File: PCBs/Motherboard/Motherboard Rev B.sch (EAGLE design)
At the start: 36 parts, among them IC1 AD590ZR, IC2 AD590ZR, Q1 32kHZ, U1 Value

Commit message: Updated pin-mappings, added SD card
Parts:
- added C18: 0.1uF, adafruit:C-USC0603
- added C19: 10uF, adafruit:C-USC0603
- added J1: (no value), sdCard:SDCARD
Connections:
- removed net 3.3V: C1.1, C10.1, C11.1, C15.1, C2.1, C3.1, C5.1, C6.1, C7.1, C8.1, C9.1, R4.2, U$1.3V3@2, U$2.RESV, U$2.VDD, U$2.VDDIO, U1.AVCC1, U1.DVCC1, U1.DVCC2, U1.DVCC3
- removed net 5V: C16.1, C17.1, IC1.+, IC2.+, U$1.5V@2
- removed net VCC: R1.2, R3.2, R7.2, R9.2
- new net SW10: C18.1, C2.1, R1.2, R3.2, R7.2, R9.2, U$1.IO.28, U$2.RESV, U$2.VDD
- new net SW5: C16.1, C17.1, IC1.+, IC2.+, U$1.IO.35
- new net SW8: C1.1, C10.1, C11.1, C15.1, C19.1, C3.1, C5.1, C6.1, C7.1, C8.1, C9.1, J1.VDD, R4.2, U$1.IO.30, U$2.VDDIO, U1.AVCC1, U1.DVCC1, U1.DVCC2, U1.DVCC3
- net GND: now also C18.2, C19.2
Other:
- note added: "SD Card Reader"
- moved on the sheet: C15, C16, C17, C2, C3, C4, IC1, IC2, R1, R10, R11, R2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

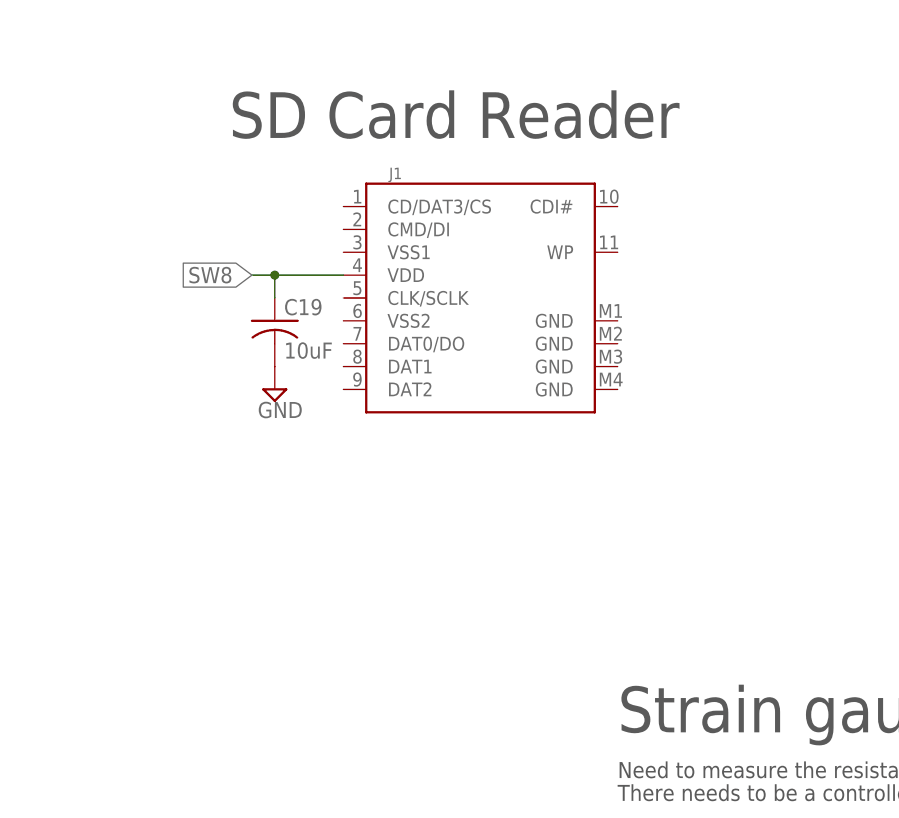
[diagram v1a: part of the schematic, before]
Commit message: Changed SD card connector
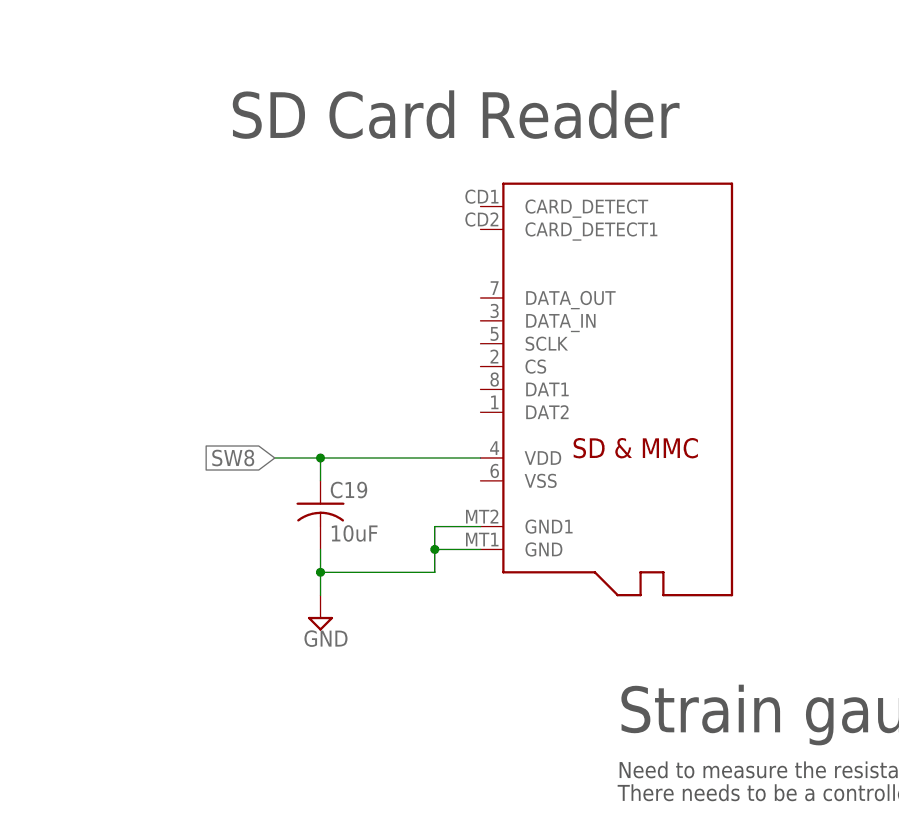
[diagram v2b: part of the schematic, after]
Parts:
- removed J1: (no value), sdCard:SDCARD
- added U$11: MICROSD, adafruit:MICROSD
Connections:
- net GND: now also U$11.GND, U$11.GND1
- net SW8: now also U$11.VDD; no longer J1.VDD
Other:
- moved on the sheet: C19

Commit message: Add temp sensors to GPS and Radio boards
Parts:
- removed IC1, IC2: AD590ZR, linear4:AD590ZR
- removed R10: RCAL, SparkFun-Resistors:12.1KOHM-0603-1/10W-1%
- removed R11: 950, SparkFun-Resistors:12.1KOHM-0603-1/10W-1%
- added R12: RCAL, SparkFun-Resistors:12.1KOHM-0603-1/10W-1%
- added R13: 950, SparkFun-Resistors:12.1KOHM-0603-1/10W-1%
- added X1, X2: OPAMP, ngspice-simulation:OPAMP
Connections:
- removed net N$8: R10.1, R11.2
- new net N$4: R12.1, R13.2
- new net TEMP1: R5.2, U$1.IO.23, X1.P
- new net TEMP2: R12.2, U$1.1O.21, X2.P
- net ADC2: now also X1.N, X1.VOUT; no longer IC1.-, R5.2
- net ADC4: now also X2.N, X2.VOUT; no longer IC2.-, R10.2
- net AGND: now also R13.1; no longer R11.1
- net SW5: no longer IC1.+, IC2.+
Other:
- note added: "AD590KRZ Temp sensor"
- note removed: "AD590KF Temp sensor"
- moved on the sheet: R5, R6

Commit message: Updated mobo, began mobo layout
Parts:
- added U$3: FDN340P, FDN340P:FDN340P
- C15: value 10uF -> 47uF
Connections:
- net SS renamed SS_IMU
- new net SD_ENABLE: U$3.G, U1.P4.3_A11
- new net SS_SD: U$11.CS
- new net VDD: C19.1, U$11.VDD, U$3.S
- net AGND: now also C1.2, C5.2, U$1.IO.26, U$1.IO.27, U$1.IO.31, U$1.IO.34, U$1.IO.39; no longer C10.2, C11.2, U$1.AGND
- net GND: now also C10.2, C11.2, U$1.GND@1, U$11.VSS; no longer C1.2, C5.2
- net MISO: now also U$11.DATA_OUT
- net MOSI: now also U$11.DATA_IN
- net SCLK: now also U$11.SCLK
- net SW10: now also C3.1, U$2.VDDIO
- net SW8: now also U$3.D; no longer C19.1, C3.1, U$11.VDD, U$2.VDDIO
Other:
- moved on the sheet: C1, C10, C11, C19, C5, C6, C7, C8, C9

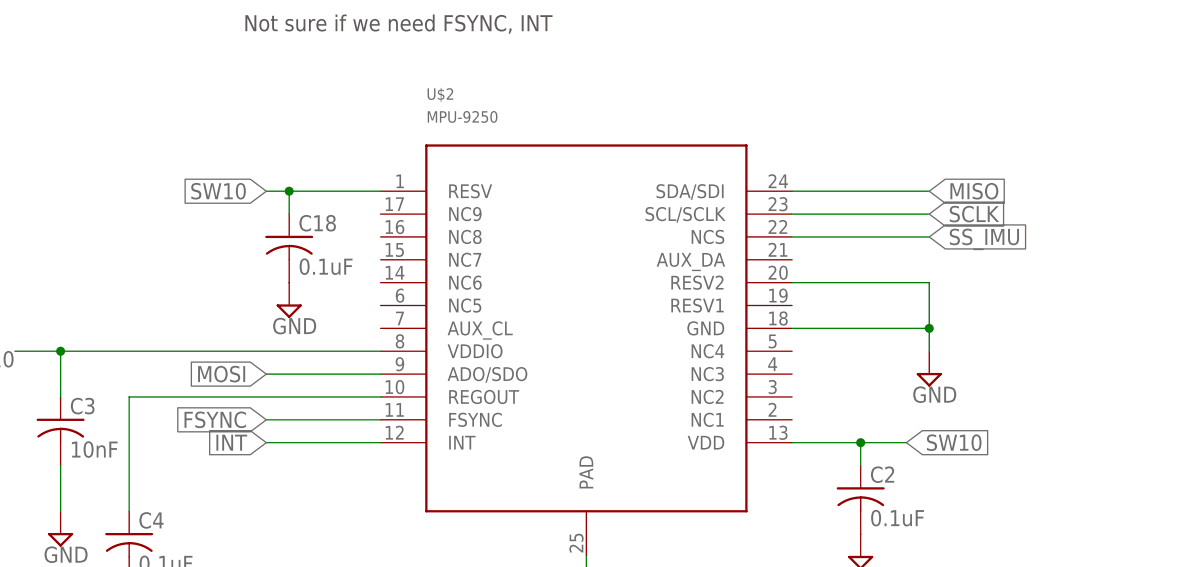
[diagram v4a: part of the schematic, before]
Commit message: Corrected IMU pinout
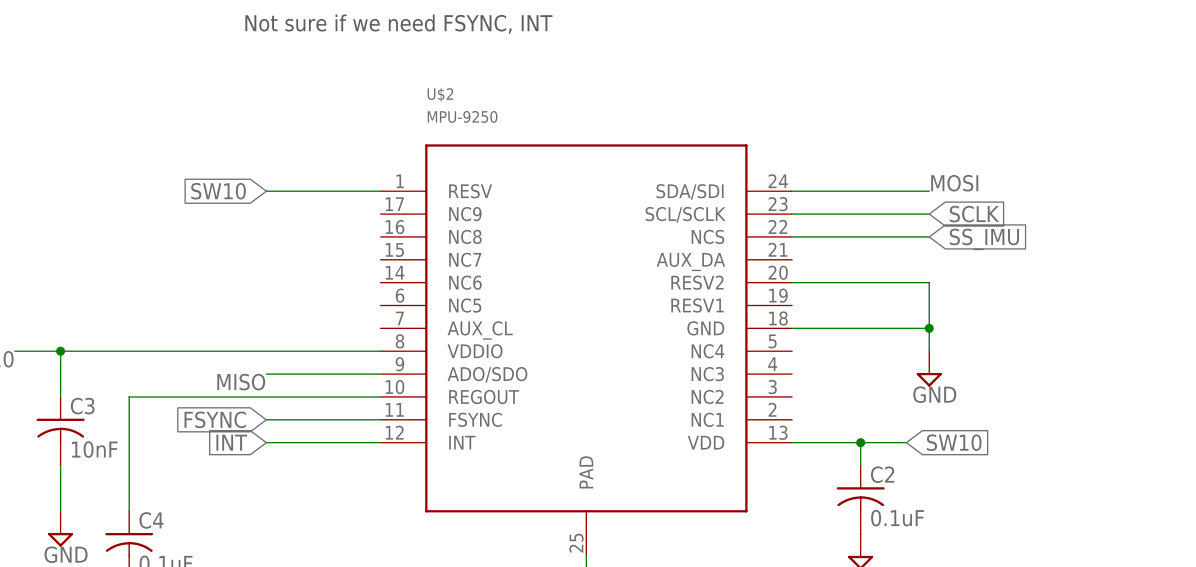
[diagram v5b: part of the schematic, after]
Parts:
- removed C18: 0.1uF, adafruit:C-USC0603
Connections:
- net GND: no longer C18.2
- net MISO: now also U$2.ADO/SDO; no longer U$2.SDA/SDI
- net MOSI: now also U$2.SDA/SDI; no longer U$2.ADO/SDO
- net SW10: no longer C18.1
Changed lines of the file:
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@@
 <part name="STRAIN_GAUGE1" library="pinhead" library_urn="urn:adsk.eagle:library:325" deviceset="PINHD-1X2" device="" package3d_urn="urn:adsk.eagle:package:22435/2"/>
 <part name="U$9" library="SparkFun-PowerSymbols" deviceset="AGND" device=""/>
-<part name="C18" library="adafruit" deviceset="C-US" device="C0603" value="0.1uF"/>
-<part name="SUPPLY19" library="supply2" library_urn="urn:adsk.eagle:library:372" deviceset="GND" device=""/>
 <part name="C2" library="adafruit" deviceset="C-US" device="C0603" value="0.1uF"/>
 <part name="SUPPLY3" library="supply2" library_urn="urn:adsk.eagle:library:372" deviceset="GND" device=""/>
@@
 <instance part="STRAIN_GAUGE1" gate="G$1" x="525.78" y="-81.28"/>
 <instance part="U$9" gate="G$1" x="497.84" y="-104.14"/>
-<instance part="C18" gate="G$1" x="256.54" y="-60.96"/>
-<instance part="SUPPLY19" gate="GND" x="256.54" y="-68.58"/>
 <instance part="C2" gate="G$1" x="320.04" y="-88.9"/>
 <instance part="SUPPLY3" gate="GND" x="320.04" y="-96.52"/>
@@
 </segment>
 <segment>
-<pinref part="C18" gate="G$1" pin="2"/>
-<pinref part="SUPPLY19" gate="GND" pin="GND"/>
-</segment>
-<segment>
 <pinref part="C2" gate="G$1" pin="2"/>
 <pinref part="SUPPLY3" gate="GND" pin="GND"/>
@@
 </segment>
 <segment>
-<pinref part="U$2" gate="G$1" pin="ADO/SDO"/>
-<wire x1="266.7" y1="-76.2" x2="254" y2="-76.2" width="0.1524" layer="91"/>
-<label x="254" y="-76.2" size="1.778" layer="95" rot="R180" xref="yes"/>
-</segment>
-<segment>
 <pinref part="U$11" gate="G$1" pin="DATA_IN"/>
 <wire x1="401.32" y1="22.86" x2="378.46" y2="22.86" width="0.1524" layer="91"/>
 <label x="378.46" y="22.86" size="1.778" layer="95" rot="R180"/>
 </segment>
+<segment>
+<pinref part="U$2" gate="G$1" pin="SDA/SDI"/>
+<wire x1="312.42" y1="-55.88" x2="327.66" y2="-55.88" width="0.1524" layer="91"/>
+<label x="327.66" y="-55.88" size="1.778" layer="95"/>
+</segment>
 </net>
 <net name="MISO" class="0">
@@
 </segment>
 <segment>
-<pinref part="U$2" gate="G$1" pin="SDA/SDI"/>
-<wire x1="312.42" y1="-55.88" x2="327.66" y2="-55.88" width="0.1524" layer="91"/>
-<label x="327.66" y="-55.88" size="1.778" layer="95" xref="yes"/>
-</segment>
-<segment>
 <pinref part="U$11" gate="G$1" pin="DATA_OUT"/>
 <wire x1="401.32" y1="25.4" x2="378.46" y2="25.4" width="0.1524" layer="91"/>
 <label x="378.46" y="25.4" size="1.778" layer="95" rot="R180"/>
+</segment>
+<segment>
+<pinref part="U$2" gate="G$1" pin="ADO/SDO"/>
+<wire x1="266.7" y1="-76.2" x2="254" y2="-76.2" width="0.1524" layer="91"/>
+<label x="254" y="-76.2" size="1.778" layer="95" rot="R180"/>
 </segment>
 </net>
@@
 <segment>
 <pinref part="U$2" gate="G$1" pin="RESV"/>
-<wire x1="266.7" y1="-55.88" x2="256.54" y2="-55.88" width="0.1524" layer="91"/>
+<wire x1="266.7" y1="-55.88" x2="254" y2="-55.88" width="0.1524" layer="91"/>
 <label x="254" y="-55.88" size="1.778" layer="95" rot="R180" xref="yes"/>
-<pinref part="C18" gate="G$1" pin="1"/>
-<wire x1="256.54" y1="-55.88" x2="254" y2="-55.88" width="0.1524" layer="91"/>
-<wire x1="256.54" y1="-58.42" x2="256.54" y2="-55.88" width="0.1524" layer="91"/>
-<junction x="256.54" y="-55.88"/>
-</segment>
-<segment>
+</segment>
+<segment>

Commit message: First working draft... still missing sensing and JTAG elements
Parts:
- removed C16: 10uF, adafruit:C-USC0603
- removed C17: 0.1uF, adafruit:C-USC0603
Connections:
- removed net SW5: C16.1, C17.1, U$1.IO.35
- new net CARD_DET1: U$11.CARD_DETECT
- new net CARD_DET2: U$11.CARD_DETECT1
- new net JTAG_CLK: U1.PJ.3_TCK_SRCPUOFF_C9
- new net JTAG_DI: U1.PJ.1_TDI_TCLK_MCLK_SRSCG0_C7
- new net JTAG_DO: U1.PJ.0_TDO_TB0OUTH_SMCLK_SRSCG1_C6
- new net JTAG_ENABLE: U1.TEST_SBWTCK
- new net JTAG_STATE: U1.PJ.2_TMS_ACLK_SROSCOFF_C8
- net AGND: no longer U$1.IO.27
- net GND: now also U$1.IO.27; no longer C16.2, C17.2
- net LITHIUM_RX: now also U1.P2.1_TB0.0_UCA0RXD_UCA0SOMI
- net LITHIUM_TX: now also U1.P2.0_TB0.6_UCA0TXD_UCA0SIMO_TB0CLK_ACLK
- net PINAVL1_RX: now also U1.P2.2_TB0.2_UCB0CLK; no longer U1.P2.0_TB0.6_UCA0TXD_UCA0SIMO_TB0CLK_ACLK
- net PINAVL1_TX: now also U1.P8.1; no longer U1.P2.1_TB0.0_UCA0RXD_UCA0SOMI
- net SD_ENABLE: now also U1.P7.2_UCB2CLK; no longer U1.P4.3_A11
- net SS_SD: now also U1.P2.7
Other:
- moved on the sheet: C15

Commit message: Replace motherboard footprint with new library
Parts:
- removed C14: 2.2nF, SparkFun-Capacitors:560PF-0603-50V-5%
- removed C19: 10uF, adafruit:C-USC0603
- removed R12: RCAL, SparkFun-Resistors:12.1KOHM-0603-1/10W-1%
- removed R13, R6: 950, SparkFun-Resistors:12.1KOHM-0603-1/10W-1%
- removed R7, R8, R9: 350, SparkFun-Resistors:12.1KOHM-0603-1/10W-1%
- removed STRAIN_GAUGE, STRAIN_GAUGE1: (no value), pinhead:PINHD-1X2
- removed U$3: FDN340P, FDN340P:FDN340P
- removed X1, X2: OPAMP, ngspice-simulation:OPAMP
- added C16: 0.1uF, resistor:C-USC0805
- added C17, C18: 10pF, resistor:C-USC0805
- added JTAG: 2514-5, con-3m:2514-5
- added U2: TPS22942DCKR, TPS22942:TPS22942DCKR
- C1, C10, C11, C2, C3, C4, C5, C6, C7, C8, C9: device adafruit:C-USC0603 -> adafruit:C-USC0805
- C12: value 10pF -> 2.2nF; device SparkFun-Capacitors:560PF-0603-50V-5% -> resistor:C-USC0805
- C13: value 10pF -> 10uF; device SparkFun-Capacitors:560PF-0603-50V-5% -> resistor:C-USC0805
- C15: value 47uF -> 10uF; device adafruit:C-USC0603 -> adafruit:C-USC0805
- R1: value 350 -> 47k; device SparkFun-Resistors:12.1KOHM-0603-1/10W-1% -> resistor:R-US_R0805
- R2, R3: value 350 -> 100k; device SparkFun-Resistors:12.1KOHM-0603-1/10W-1% -> resistor:R-US_R0805
- R4: value 47K -> 0; device SparkFun-Resistors:12.1KOHM-0603-1/10W-1% -> resistor:R-US_R0805
- R5: value RCAL -> 47k; device SparkFun-Resistors:12.1KOHM-0603-1/10W-1% -> resistor:R-US_R0805
- U$1: value PC104 -> PC104_MOBO; device Cubesat:PC104 -> Cubesat:PC104_MOBO
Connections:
- removed net ADC1: R3.1, STRAIN_GAUGE.1, U1.P1.0_TA0.1_DMAE0_RTCCLK_A0_C0_VREF-_VEREF-
- removed net ADC2: U1.P1.1_TA0.2_TA1CLK_COUT_A1_C1_VREF+_VEREF+, X1.N, X1.VOUT
- removed net ADC3: R9.1, STRAIN_GAUGE1.1, U1.P1.2_TA1.1_TA0CLK_COUT_A2_C2
- removed net ADC4: U1.P1.3_TA1.2_UCB0STE_A3_C3, X2.N, X2.VOUT
- removed net CARD_DET1: U$11.CARD_DETECT
- removed net CARD_DET2: U$11.CARD_DETECT1
- removed net FSYNC: U$2.FSYNC
- removed net JTAG_CLK: U1.PJ.3_TCK_SRCPUOFF_C9
- removed net JTAG_DI: U1.PJ.1_TDI_TCLK_MCLK_SRSCG0_C7
- removed net JTAG_DO: U1.PJ.0_TDO_TB0OUTH_SMCLK_SRSCG1_C6
- removed net JTAG_ENABLE: U1.TEST_SBWTCK
- removed net JTAG_STATE: U1.PJ.2_TMS_ACLK_SROSCOFF_C8
- removed net N$6: R7.1, R8.2
- removed net N$7: C14.2, R4.1, U1.RST_NMI_SBWTDIO_N
- removed net N$9: R5.1, R6.2
- removed net SD_ENABLE: U$3.G, U1.P7.2_UCB2CLK
- removed net SS_IMU: U$2.NCS, U1.P2.3_TA0.0_UCA1STE_A6_C10
- removed net SS_SD: U$11.CS, U1.P2.7
- removed net SW8: C1.1, C10.1, C11.1, C15.1, C5.1, C6.1, C7.1, C8.1, C9.1, R4.2, U$1.IO.30, U$3.D, U1.AVCC1, U1.DVCC1, U1.DVCC2, U1.DVCC3
- removed net TEMP1: R5.2, U$1.IO.23, X1.P
- removed net TEMP2: R12.2, U$1.1O.21, X2.P
- removed net VDD: C19.1, U$11.VDD, U$3.S
- new net 3V3: C13.1, C15.1, C16.1, R1.1, R2.1, U$1.3V3BUS1, U$11.VDD, U2.VIN
- new net 3V3_UC: C1.1, C10.1, C11.1, C5.1, C6.1, C7.1, C8.1, C9.1, R5.2, U1.AVCC1, U1.DVCC1, U1.DVCC2, U1.DVCC3, U2.VOUT
- new net CS_IMU: U$2.NCS, U1.P8.0
- new net CS_SD: R1.2, U$11.CS, U1.P1.3_TA1.2_UCB0STE_A3_C3
- new net DNU_TEMP_ADC: U1.P3.0_A12_C12
- new net LI_OA_RESET: R4.1, U$1.LI_OA_RST
- new net RST: C12.1, JTAG-11.KL, R5.1, U1.RST_NMI_SBWTDIO_N
- new net TCK: JTAG-7.KL, U1.PJ.3_TCK_SRCPUOFF_C9
- new net TDI: JTAG-3.KL, U1.PJ.1_TDI_TCLK_MCLK_SRSCG0_C7
- new net TDO: JTAG-1.KL, U1.PJ.0_TDO_TB0OUTH_SMCLK_SRSCG1_C6
- new net TEST: JTAG-8.KL, U1.TEST_SBWTCK
- new net TMS: JTAG-5.KL, U1.PJ.2_TMS_ACLK_SROSCOFF_C8
- net AGND: now also U$1.GND1, U$1.GND2, U$1.GND3, U$1.GND5; no longer R13.1, R2.1, R6.1, R8.1, STRAIN_GAUGE.2, STRAIN_GAUGE1.2, U$1.IO.26, U$1.IO.31, U$1.IO.34, U$1.IO.39
- net GND: now also C12.2, C13.2, C16.2, C17.2, C18.2, JTAG-9.KL, R3.1, U$1.GND10, U$1.GND4, U$1.GND6, U$1.GND7, U$1.GND8, U$1.GND9, U$2.FSYNC, U2.GND; no longer C12.1, C13.1, C14.1, C19.2, U$1.GND@1, U$1.GND@2, U$1.GND@3, U$1.IO.27
- net LITHIUM_RX: now also U$1.LI_RX, U1.P5.5_UCA2RXD_UCA2SOMI_ACLK; no longer U$1.P$37, U1.P2.1_TB0.0_UCA0RXD_UCA0SOMI
- net LITHIUM_TX: now also U$1.LI_TX, U1.P5.4_UCA2TXD_UCA2SIMO_TB0OUTH; no longer U$1.P$39, U1.P2.0_TB0.6_UCA0TXD_UCA0SIMO_TB0CLK_ACLK
- net MISO: now also U1.P1.7_TB0.4_UCB0SOMI_UCB0SCL_TA1.0; no longer U1.P2.6_TB0.1_UCA1RXD_UCA1SOMI
- net MOSI: now also U1.P1.6_TB0.3_UCB0SIMO_UCB0SDA_TA0.0; no longer U1.P2.5_TB0.0_UCA1TXD_UCA1SIMO
- net N$1: now also R2.2, U2.OC; no longer C12.2, Q1.2, U1.PJ.5_LFXOUT
- net N$2: now also C17.1, Q1.2, U1.PJ.5_LFXOUT; no longer R1.1, R2.2
- net N$4: now also C18.1, Q1.1, U1.PJ.7_HFXOUT; no longer R12.1, R13.2
- net N$5: now also R3.2, R4.2, U2.ON; no longer C13.2, Q1.1, U1.PJ.7_HFXOUT
- net PINAVL1_RX: now also U$1.GPS_RX, U1.P2.1_TB0.0_UCA0RXD_UCA0SOMI; no longer U$1.P$35, U1.P2.2_TB0.2_UCB0CLK
- net PINAVL1_TX: now also U$1.GPS_TX, U1.P2.0_TB0.6_UCA0TXD_UCA0SIMO_TB0CLK_ACLK; no longer U$1.P$33, U1.P8.1
- net SCL: now also U$1.I2C_CLK, U1.P7.1_UCB2SOMI_UCB2SCL; no longer U$1.I2C-SCL, U1.P1.7_TB0.4_UCB0SOMI_UCB0SCL_TA1.0
- net SCLK: now also U1.P2.2_TB0.2_UCB0CLK; no longer U1.P2.4_TA1.0_UCA1CLK_A7_C11
- net SDA: now also U$1.I2C_DATA, U1.P7.0_UCB2SIMO_UCB2SDA; no longer U$1.I2C-SDA, U1.P1.6_TB0.3_UCB0SIMO_UCB0SDA_TA0.0
- net SW10: now also U$1.SW10_3V3; no longer R1.2, R3.2, R7.2, R9.2, U$1.IO.28
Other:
- note added: "JTAG Interface"
- note added: "MSP430FR5994 Processor"
- note added: "Need to add a jumper on pins 2 & 4 to control power flow!"
- note removed: "AD590KRZ Temp sensor"
- note removed: "MSP430FR59xx Processor"
- note removed: "Need to measure the resistance of the wires leading from the header to the gauge."
- note removed: "RCAL will have to be determined to eliminate the calibration error"
- note removed: "Strain gauges"
- note removed: "There needs to be a controlled impedence implemented on the otherside of this wheatstone bridge to equal it out."
- moved on the sheet: C12, C13, C15, C2, C3, C4, Q1, R1, R2, R3, R4, R5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

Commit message: Use common PC104 footprint with dimensions set per board
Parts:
- U$1: value PC104_MOBO -> PC104_NO_DIMENSION; device Cubesat:PC104_MOBO -> Cubesat:PC104_NO_DIMENSION
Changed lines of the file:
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@@
 <part name="SUPPLY21" library="supply2" library_urn="urn:adsk.eagle:library:372" deviceset="GND" device=""/>
 <part name="R4" library="resistor" library_urn="urn:adsk.eagle:library:348" deviceset="R-US_" device="R0805" package3d_urn="urn:adsk.eagle:package:23553/2" value="0"/>
-<part name="U$1" library="Cubesat" deviceset="PC104_MOBO" device=""/>
+<part name="U$1" library="Cubesat" deviceset="PC104_NO_DIMENSION" device=""/>
 </parts>
 <sheets>
